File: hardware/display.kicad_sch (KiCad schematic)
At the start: 5 parts, among them J1 Conn_02x20_Odd_Even_Shielded

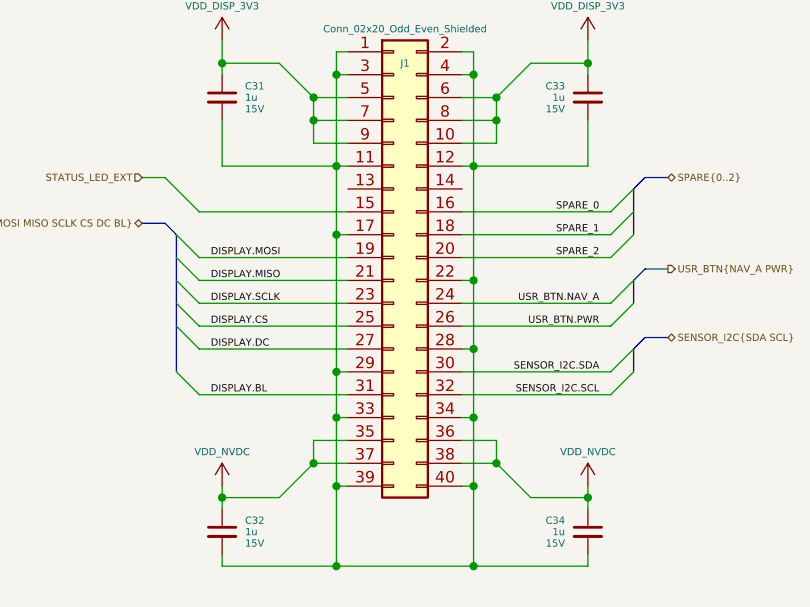
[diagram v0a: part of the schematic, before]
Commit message: minor sch tweaks, more layout, added power emc shield
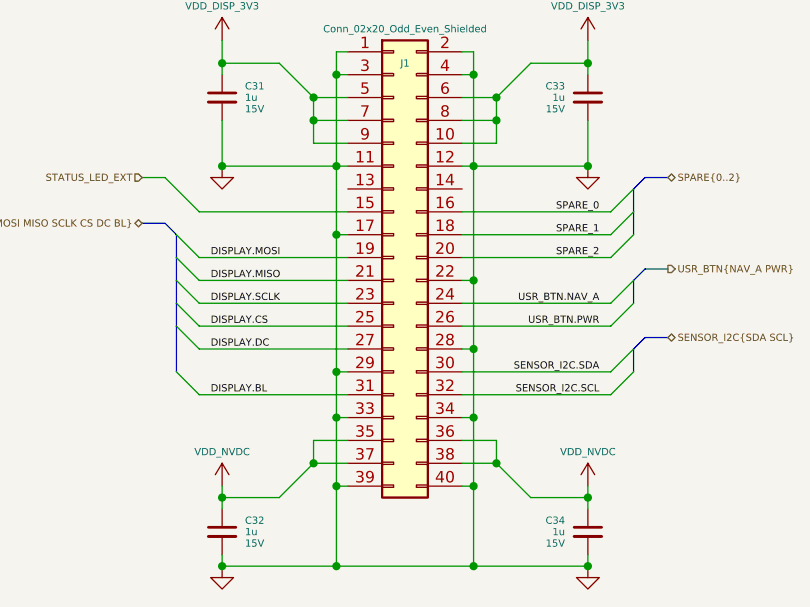
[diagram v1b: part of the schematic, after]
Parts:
- C31, C32, C33, C34: footprint Capacitor_SMD:C_0603_1608Metric -> Capacitor_SMD:C_0402_1005Metric
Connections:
- net GND: now reaches C31.2, C32.2, C33.2, C34.2, J1.1 (Pin_1), J1.11 (Pin_11), J1.12 (Pin_12), J1.17 (Pin_17), J1.2 (Pin_2), J1.22 (Pin_22), J1.28 (Pin_28), J1.29 (Pin_29), J1.3 (Pin_3), J1.33 (Pin_33), J1.34 (Pin_34), J1.39 (Pin_39), J1.4 (Pin_4), J1.40 (Pin_40)
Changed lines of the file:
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@@
   (junction (at 140.97 102.87) (diameter 0) (color 0 0 0 0)
   )
+  (junction (at 168.91 95.25) (diameter 0) (color 0 0 0 0)
+  )
   (junction (at 138.43 90.17) (diameter 0) (color 0 0 0 0)
   )
   (junction (at 156.21 107.95) (diameter 0) (color 0 0 0 0)
   )
+  (junction (at 128.27 95.25) (diameter 0) (color 0 0 0 0)
+  )
   (junction (at 158.75 90.17) (diameter 0) (color 0 0 0 0)
   )
@@
   )
   (junction (at 128.27 132.08) (diameter 0) (color 0 0 0 0)
+  )
+  (junction (at 168.91 139.7) (diameter 0) (color 0 0 0 0)
+  )
+  (junction (at 128.27 139.7) (diameter 0) (color 0 0 0 0)
   )
   (bus_entry (at 125.73 120.65) (size -2.54 -2.54)
@@
   (hierarchical_label "STATUS_LED_EXT" (shape input) (at 119.38 96.52 180)
     (effects (font (size 0.8 0.8)) (justify right))
+  )
+  (symbol (lib_id "power:GND") (at 168.91 139.7 0) (unit 1)
+    (in_bom yes) (on_board yes) (fields_autoplaced)
+    (property "Reference" "#PWR0104" (id 0) (at 168.91 146.05 0)
+      (effects (font (size 0.8 0.8)) hide)
+    )
+    (property "Value" "GND" (id 1) (at 168.91 144.78 0)
+      (effects (font (size 0.8 0.8)) hide)
+    )
+    (property "Footprint" "" (id 2) (at 168.91 139.7 0)
+      (effects (font (size 0.8 0.8)) hide)
+    )
+    (property "Datasheet" "" (id 3) (at 168.91 139.7 0)
+      (effects (font (size 0.8 0.8)) hide)
+    )
+    (pin "1")
   )
   (symbol (lib_id "bt_power:VDD_DISP_3V3") (at 128.27 81.28 0) (unit 1)
@@
       (effects (font (size 0.8 0.8)) (justify left))
     )
-    (property "Footprint" "Capacitor_SMD:C_0603_1608Metric" (id 2) (at 128.27 135.89 0)
+    (property "Footprint" "Capacitor_SMD:C_0402_1005Metric" (id 2) (at 128.27 135.89 0)
       (effects (font (size 0.8 0.8)) hide)
     )
@@
       (effects (font (size 0.8 0.8)) (justify left))
     )
-    (property "Footprint" "Capacitor_SMD:C_0603_1608Metric" (id 2) (at 168.91 135.89 0)
+    (property "Footprint" "Capacitor_SMD:C_0402_1005Metric" (id 2) (at 168.91 135.89 0)
       (effects (font (size 0.8 0.8)) hide)
     )
@@
       (effects (font (size 0.8 0.8)) (justify left))
     )
-    (property "Footprint" "Capacitor_SMD:C_0603_1608Metric" (id 2) (at 168.91 87.63 0)
+    (property "Footprint" "Capacitor_SMD:C_0402_1005Metric" (id 2) (at 168.91 87.63 0)
       (effects (font (size 0.8 0.8)) hide)
     )
@@
     (pin "1")
     (pin "2")
+  )
+  (symbol (lib_id "power:GND") (at 128.27 139.7 0) (unit 1)
+    (in_bom yes) (on_board yes) (fields_autoplaced)
+    (property "Reference" "#PWR0106" (id 0) (at 128.27 146.05 0)
+      (effects (font (size 0.8 0.8)) hide)
+    )
+    (property "Value" "GND" (id 1) (at 128.27 144.78 0)
+      (effects (font (size 0.8 0.8)) hide)
+    )
+    (property "Footprint" "" (id 2) (at 128.27 139.7 0)
+      (effects (font (size 0.8 0.8)) hide)
+    )
+    (property "Datasheet" "" (id 3) (at 128.27 139.7 0)
+      (effects (font (size 0.8 0.8)) hide)
+    )
+    (pin "1")
   )
   (symbol (lib_id "Device:C_Small") (at 128.27 87.63 0) (unit 1)
@@
       (effects (font (size 0.8 0.8)) (justify left))
     )
-    (property "Footprint" "Capacitor_SMD:C_0603_1608Metric" (id 2) (at 128.27 87.63 0)
+    (property "Footprint" "Capacitor_SMD:C_0402_1005Metric" (id 2) (at 128.27 87.63 0)
       (effects (font (size 0.8 0.8)) hide)
     )
@@
     (pin "2")
   )
+  (symbol (lib_id "power:GND") (at 168.91 95.25 0) (unit 1)
+    (in_bom yes) (on_board yes) (fields_autoplaced)
+    (property "Reference" "#PWR0116" (id 0) (at 168.91 101.6 0)
+      (effects (font (size 0.8 0.8)) hide)
+    )
+    (property "Value" "GND" (id 1) (at 168.91 100.33 0)
+      (effects (font (size 0.8 0.8)) hide)
+    )
+    (property "Footprint" "" (id 2) (at 168.91 95.25 0)
+      (effects (font (size 0.8 0.8)) hide)
+    )
+    (property "Datasheet" "" (id 3) (at 168.91 95.25 0)
+      (effects (font (size 0.8 0.8)) hide)
+    )
+    (pin "1")
+  )
+  (symbol (lib_id "power:GND") (at 128.27 95.25 0) (unit 1)
+    (in_bom yes) (on_board yes) (fields_autoplaced)
+    (property "Reference" "#PWR0120" (id 0) (at 128.27 101.6 0)
+      (effects (font (size 0.8 0.8)) hide)
+    )
+    (property "Value" "GND" (id 1) (at 128.27 100.33 0)
+      (effects (font (size 0.8 0.8)) hide)
+    )
+    (property "Footprint" "" (id 2) (at 128.27 95.25 0)
+      (effects (font (size 0.8 0.8)) hide)
+    )
+    (property "Datasheet" "" (id 3) (at 128.27 95.25 0)
+      (effects (font (size 0.8 0.8)) hide)
+    )
+    (pin "1")
+  )
   (symbol (lib_id "bt_power:VDD_NVDC") (at 128.27 130.81 0) (unit 1)

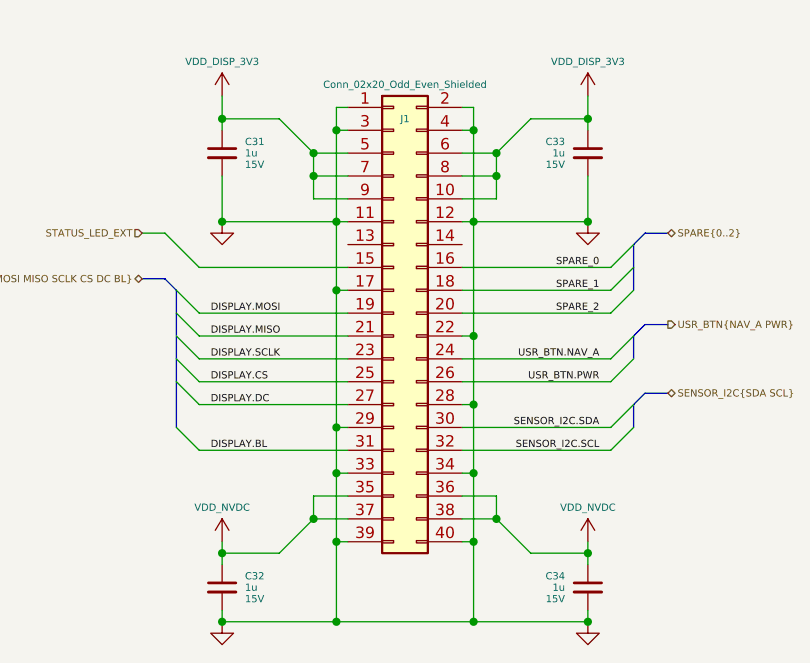
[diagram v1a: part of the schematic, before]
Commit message: screen mock, tweaked layout easier powerplane division
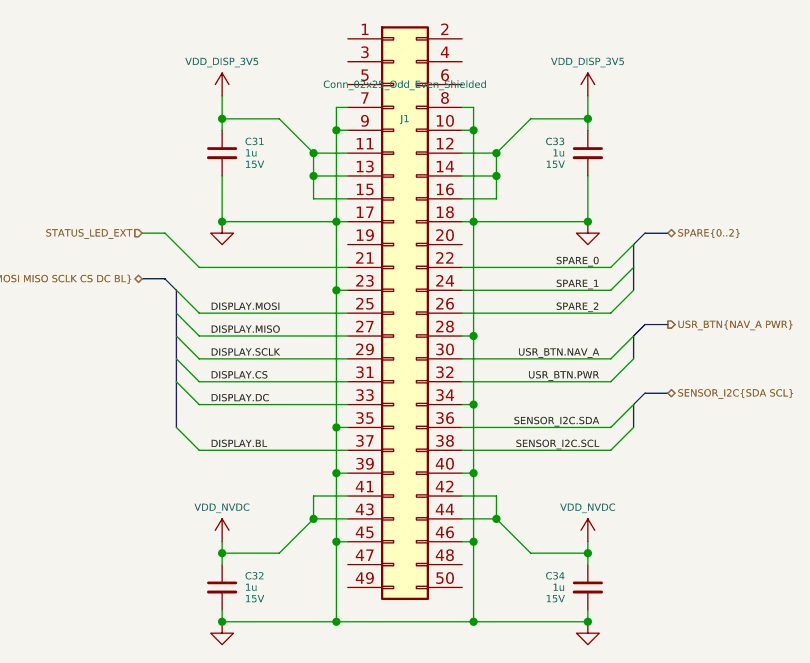
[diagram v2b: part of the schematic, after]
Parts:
- J1: value Conn_02x20_Odd_Even_Shielded -> Conn_02x25_Odd_Even_Shielded; footprint Connector_Molex:Molex_SlimStack_502426-4010_2x20_P0.40mm_Vertical -> Connector_Molex:Molex_SlimStack_55560-0501_2x25_P0.50mm_Vertical; symbol Connector_Generic:Conn_02x20_Odd_Even -> Connector_Generic:Conn_02x25_Odd_Even
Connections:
- net DISPLAY.BL: now also J1.37 (Pin_37); no longer J1.31 (Pin_31)
- net DISPLAY.CS: now also J1.31 (Pin_31); no longer J1.25 (Pin_25)
- net DISPLAY.DC: now also J1.33 (Pin_33); no longer J1.27 (Pin_27)
- net DISPLAY.MISO: now also J1.27 (Pin_27); no longer J1.21 (Pin_21)
- net DISPLAY.MOSI: now also J1.25 (Pin_25); no longer J1.19 (Pin_19)
- net DISPLAY.SCLK: now also J1.29 (Pin_29); no longer J1.23 (Pin_23)
- net GND: now also J1.10 (Pin_10), J1.18 (Pin_18), J1.23 (Pin_23), J1.35 (Pin_35), J1.45 (Pin_45), J1.46 (Pin_46), J1.7 (Pin_7), J1.8 (Pin_8), J1.9 (Pin_9); no longer J1.1 (Pin_1), J1.11 (Pin_11), J1.12 (Pin_12), J1.2 (Pin_2), J1.22 (Pin_22), J1.29 (Pin_29), J1.3 (Pin_3), J1.33 (Pin_33), J1.4 (Pin_4)
- net SENSOR_I2C.SCL: now also J1.38 (Pin_38); no longer J1.32 (Pin_32)
- net SENSOR_I2C.SDA: now also J1.36 (Pin_36); no longer J1.30 (Pin_30)
- net SPARE_0: now also J1.22 (Pin_22); no longer J1.16 (Pin_16)
- net SPARE_1: now also J1.24 (Pin_24); no longer J1.18 (Pin_18)
- net SPARE_2: now also J1.26 (Pin_26); no longer J1.20 (Pin_20)
- net STATUS_LED_EXT: now also J1.21 (Pin_21); no longer J1.15 (Pin_15)
- net USR_BTN.NAV_A: now also J1.30 (Pin_30); no longer J1.24 (Pin_24)
- net USR_BTN.PWR: now also J1.32 (Pin_32); no longer J1.26 (Pin_26)
- net VDD_NVDC: now also J1.41 (Pin_41), J1.42 (Pin_42), J1.43 (Pin_43), J1.44 (Pin_44); no longer J1.35 (Pin_35), J1.36 (Pin_36), J1.37 (Pin_37), J1.38 (Pin_38)
- net VDD_DISP_3V5: now reaches J1.13 (Pin_13)
- net VDD_DISP_3V5: now also C31.1, C33.1, J1.11 (Pin_11), J1.12 (Pin_12), J1.14 (Pin_14), J1.15 (Pin_15), J1.16 (Pin_16)
- removed net VDD_DISP_3V3: C31.1, C33.1, J1.10 (Pin_10), J1.5 (Pin_5), J1.6 (Pin_6), J1.7 (Pin_7), J1.8 (Pin_8), J1.9 (Pin_9)
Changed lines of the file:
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@@
     (effects (font (size 0.8 0.8)) (justify right))
+  )
+  (symbol (lib_id "bt_power:VDD_DISP_3V5") (at 168.91 81.28 0) (unit 1)
+    (in_bom no) (on_board no)
+    (property "Reference" "#U0105" (id 0) (at 169.4434 81.28 0)
+      (effects (font (size 1.27 1.27)) hide)
+    )
+    (property "Value" "VDD_DISP_3V5" (id 1) (at 168.91 77.47 0)
+      (effects (font (size 0.8 0.8)))
+    )
+    (property "Footprint" "" (id 2) (at 169.4434 81.28 0)
+      (effects (font (size 1.27 1.27)) hide)
+    )
+    (property "Datasheet" "" (id 3) (at 169.4434 81.28 0)
+      (effects (font (size 1.27 1.27)) hide)
+    )
+    (pin "1")
   )
   (symbol (lib_id "power:GND") (at 168.91 139.7 0) (unit 1)
@@
     (property "Datasheet" "" (id 3) (at 168.91 139.7 0)
       (effects (font (size 0.8 0.8)) hide)
-    )
-    (pin "1")
-  )
-  (symbol (lib_id "bt_power:VDD_DISP_3V3") (at 128.27 81.28 0) (unit 1)
-    (in_bom no) (on_board no)
-    (property "Reference" "#U0104" (id 0) (at 128.8034 81.28 0)
-      (effects (font (size 1.27 1.27)) hide)
-    )
-    (property "Value" "VDD_DISP_3V3" (id 1) (at 128.27 77.47 0)
-      (effects (font (size 0.8 0.8)))
-    )
-    (property "Footprint" "" (id 2) (at 128.8034 81.28 0)
-      (effects (font (size 1.27 1.27)) hide)
-    )
-    (property "Datasheet" "" (id 3) (at 128.8034 81.28 0)
-      (effects (font (size 1.27 1.27)) hide)
     )
     (pin "1")
@@
     (pin "2")
   )
-  (symbol (lib_id "bt_power:VDD_DISP_3V3") (at 168.91 81.28 0) (mirror y) (unit 1)
+  (symbol (lib_id "bt_power:VDD_DISP_3V5") (at 128.27 81.28 0) (unit 1)
     (in_bom no) (on_board no)
-    (property "Reference" "#U0105" (id 0) (at 168.3766 81.28 0)
+    (property "Reference" "#U0104" (id 0) (at 128.8034 81.28 0)
       (effects (font (size 1.27 1.27)) hide)
     )
-    (property "Value" "VDD_DISP_3V3" (id 1) (at 168.91 77.47 0)
+    (property "Value" "VDD_DISP_3V5" (id 1) (at 128.27 77.47 0)
       (effects (font (size 0.8 0.8)))
     )
-    (property "Footprint" "" (id 2) (at 168.3766 81.28 0)
+    (property "Footprint" "" (id 2) (at 128.8034 81.28 0)
       (effects (font (size 1.27 1.27)) hide)
     )
-    (property "Datasheet" "" (id 3) (at 168.3766 81.28 0)
+    (property "Datasheet" "" (id 3) (at 128.8034 81.28 0)
       (effects (font (size 1.27 1.27)) hide)
     )
     (pin "1")
   )
-  (symbol (lib_id "Connector_Generic:Conn_02x20_Odd_Even") (at 147.32 105.41 0) (unit 1)
+  (symbol (lib_id "Connector_Generic:Conn_02x25_Odd_Even") (at 147.32 105.41 0) (unit 1)
     (in_bom yes) (on_board yes)
     (property "Reference" "J1" (id 0) (at 148.59 83.82 0)
       (effects (font (size 0.8 0.8)))
     )
-    (property "Value" "Conn_02x20_Odd_Even_Shielded" (id 1) (at 148.59 80.01 0)
+    (property "Value" "Conn_02x25_Odd_Even_Shielded" (id 1) (at 148.59 80.01 0)
       (effects (font (size 0.8 0.8)))
     )
-    (property "Footprint" "Connector_Molex:Molex_SlimStack_502426-4010_2x20_P0.40mm_Vertical" (id 2) (at 147.32 105.41 0)
+    (property "Footprint" "Connector_Molex:Molex_SlimStack_55560-0501_2x25_P0.50mm_Vertical" (id 2) (at 147.32 105.41 0)
       (effects (font (size 1.27 1.27)) hide)
     )
@@
     (pin "4")
     (pin "40")
+    (pin "41")
+    (pin "42")
+    (pin "43")
+    (pin "44")
+    (pin "45")
+    (pin "46")
+    (pin "47")
+    (pin "48")
+    (pin "49")
     (pin "5")
+    (pin "50")
     (pin "6")
     (pin "7")

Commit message: Updates
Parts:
- removed C31, C32, C33, C34: 1u, Capacitor_SMD:C_0402_1005Metric, symbol Device:C_Small
- removed J1: Conn_02x25_Odd_Even_Shielded, Connector_Molex:Molex_SlimStack_55560-0501_2x25_P0.50mm_Vertical, symbol Connector_Generic:Conn_02x25_Odd_Even
